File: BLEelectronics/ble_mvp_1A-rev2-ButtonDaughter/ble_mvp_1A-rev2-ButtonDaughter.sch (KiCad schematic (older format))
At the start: 7 parts, among them J1 Nordic_nRF52840_breakout, SW1 SW_Push, SW2 SW_Push, U1 BAT-HLD-001

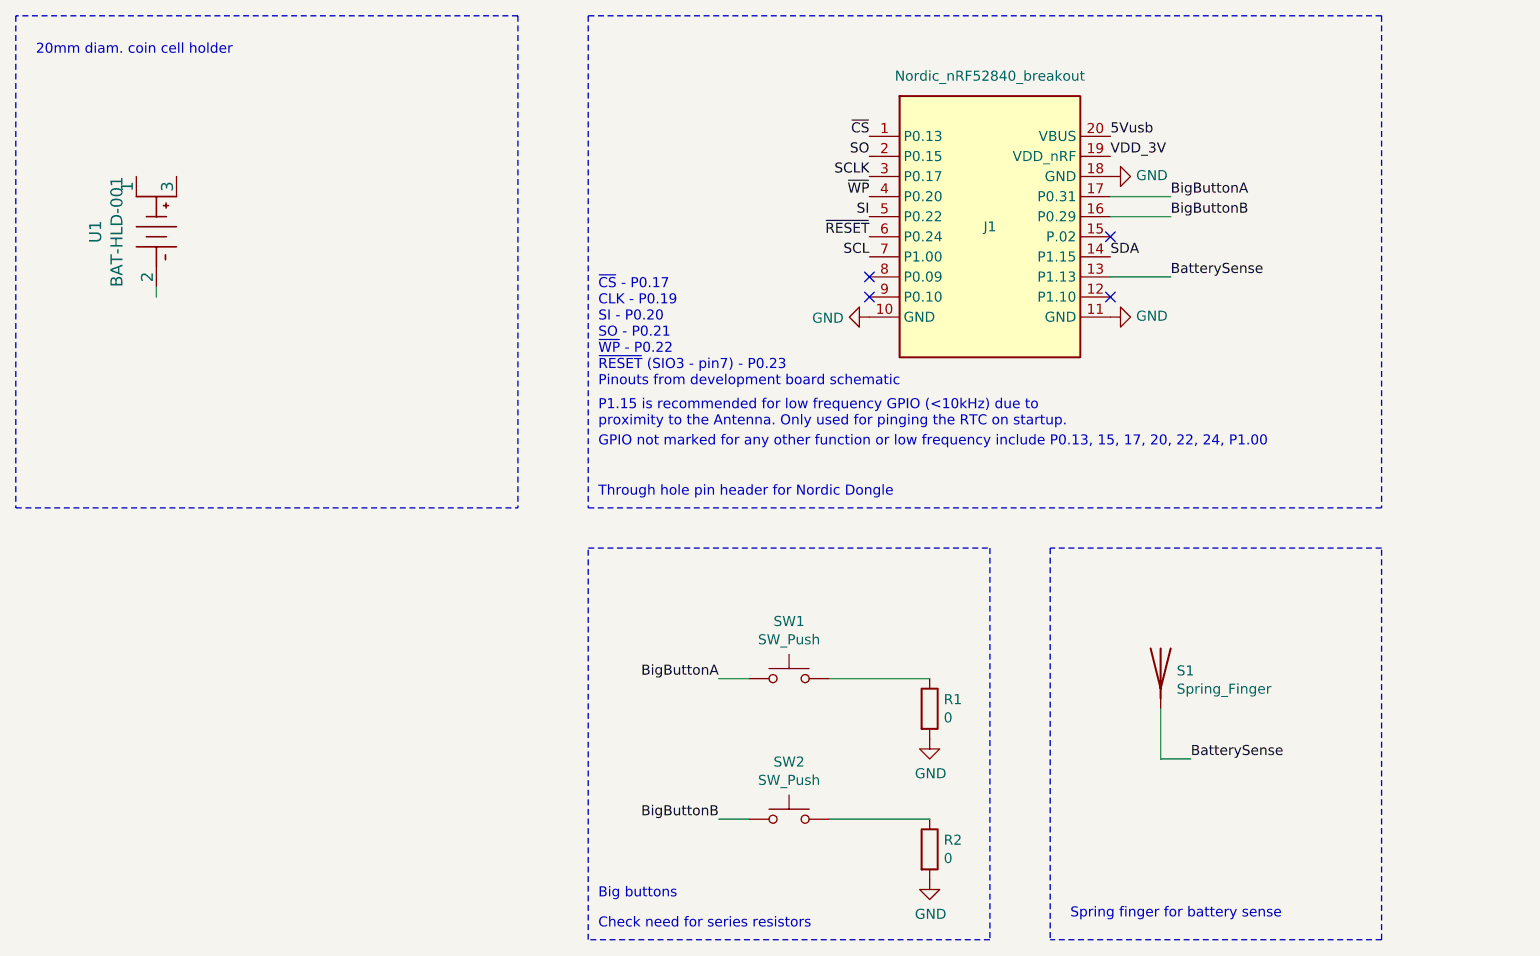
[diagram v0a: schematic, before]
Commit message: mvp1a-rev2 button daughter board schematic and layout ready for review. ToDo: BOM prep.
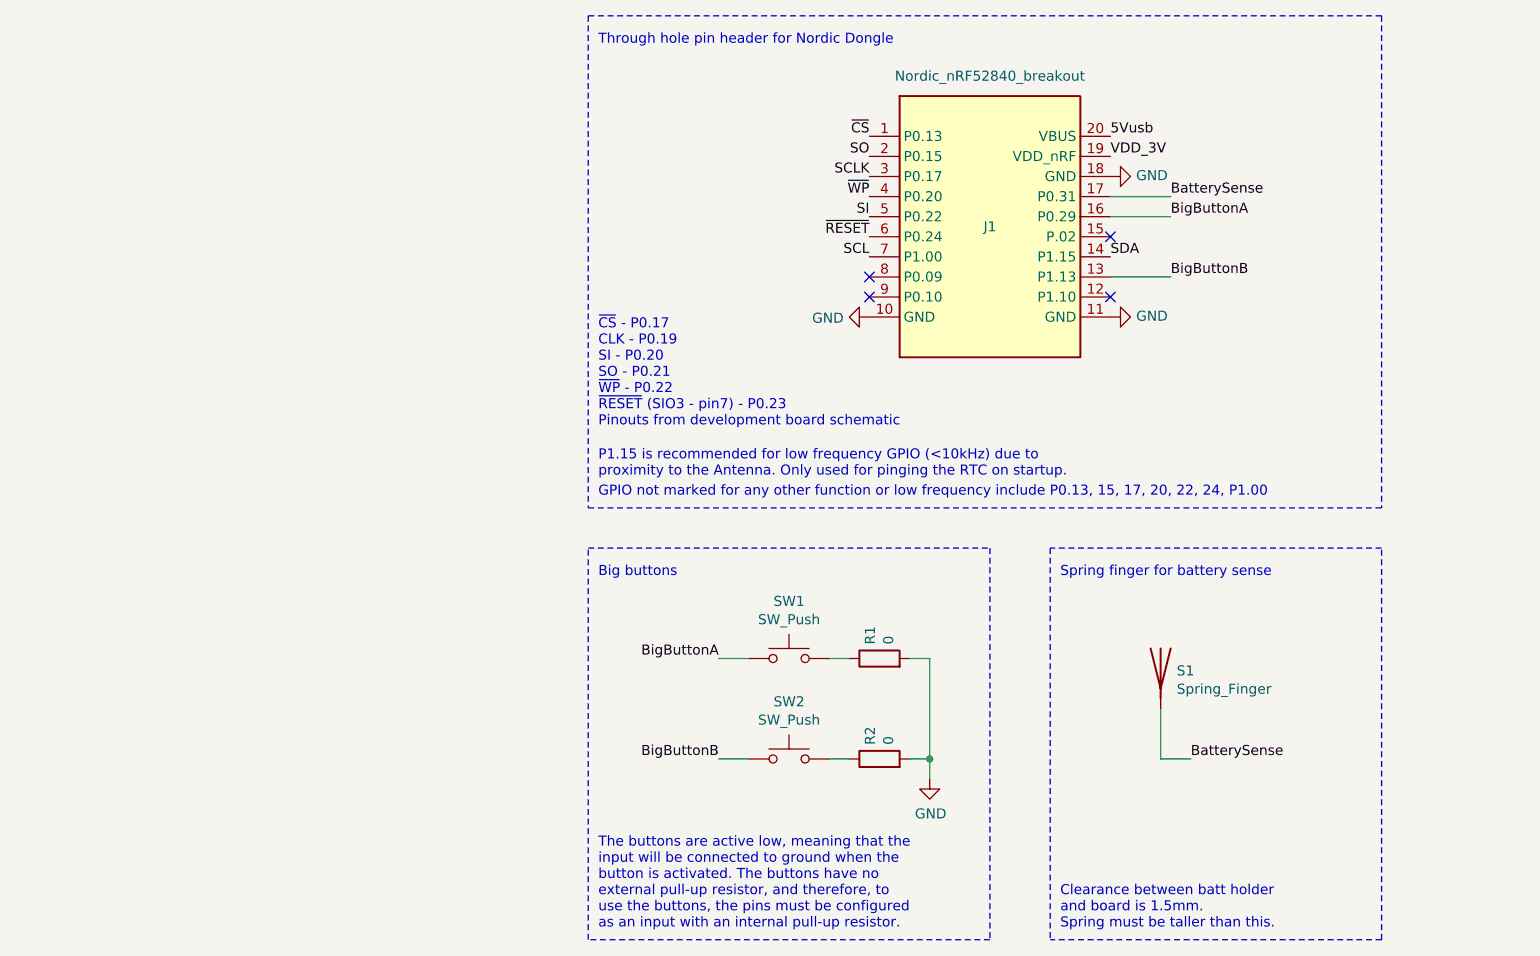
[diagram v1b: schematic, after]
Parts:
- removed U1: BAT-HLD-001, 0my_footprints:BAT-HLD-001, symbol BAT-HLD-001:BAT-HLD-001
- S1: footprint (none) -> 0my_footprints:SpringFingerGeneric; DPN (none) -> 952-2733-1-ND; MFR (none) -> Harwin Inc.; MPN (none) -> S7131-45R
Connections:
- wire segments 10 -> 13
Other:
- note added: "Clearance between batt holder \nand board is 1.5mm. \nSpring must be taller than this."
- note added: "The buttons are active low, meaning that the \ninput will be connected to ground when the\nbutton is activated. The buttons have no \nexternal pull-up resistor, and therefore, to \nuse the buttons, the pins must be configured \nas an input with an internal pull-up resistor."
- note removed: "20mm diam. coin cell holder"
- note removed: "Check need for series resistors"
- moved on the sheet: R1, R2, SW1, SW2
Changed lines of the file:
@@
 $EndDescr
 Wire Notes Line
-	1050 3350 3550 3350
-Wire Notes Line
-	3550 900  1050 900
-Wire Notes Line
 	7850 900  3900 900
 Wire Notes Line
-	3900 3350 7850 3350
-Wire Notes Line
-	3900 3550 5900 3550
-Wire Notes Line
 	5900 3550 5900 5500
 Wire Notes Line
@@
 Wire Notes Line
 	3900 900  3900 3350
-Wire Notes Line
-	3550 900  3550 3350
-Wire Notes Line
-	1050 900  1050 3350
 NoConn ~ 5300 2200
 NoConn ~ 6500 2000
 NoConn ~ 6500 2300
 NoConn ~ 5300 2300
-Text Notes 3950 3300 0    50   ~ 0
+Text Notes 3950 1050 0    50   ~ 0
 Through hole pin header for Nordic Dongle
 Text Label 6500 2100 0    50   ~ 0
@@
 Text Label 5300 2100 2    50   ~ 0
 SCL
-Text Notes 3950 2750 0    50   ~ 0
-~CS~ - P0.17\nCLK - P0.19\nSI - P0.20\nSO - P0.21\n~WP~ - P0.22\n~RESET~ (SIO3 - pin7) - P0.23\nPinouts from development board schematic\n
 Text Label 5300 2000 2    50   ~ 0
 ~RESET~
 Text Label 5300 1800 2    50   ~ 0
 ~WP~
-Text Notes 3950 2950 0    50   ~ 0
-P1.15 is recommended for low frequency GPIO (<10kHz) due to\nproximity to the Antenna. Only used for pinging the RTC on startup.
 Text Label 5300 1700 2    50   ~ 0
 SCLK
@@
 Text Label 5300 1600 2    50   ~ 0
 SO
-Text Notes 3950 3050 0    50   ~ 0
-GPIO not marked for any other function or low frequency include P0.13, 15, 17, 20, 22, 24, P1.00
 Text Label 6500 1600 0    50   ~ 0
 VDD_3V
@@
 	0    -1   -1   0
 $EndComp
-Wire Wire Line
-	1750 2300 1750 2250
-Text Notes 1150 1100 0    50   ~ 0
-20mm diam. coin cell holder
-$Comp
-L BAT-HLD-001:BAT-HLD-001 U1
-U 1 1 5E9C706C
-P 1650 1700
-F 0 "U1" H 1925 1903 60  0000 C CNN
-F 1 "BAT-HLD-001" H 1925 1797 60  0000 C CNN
-F 2 "0my_footprints:BAT-HLD-001" H 1934 1358 60  0001 C CNN
-F 3 "https://linxtechnologies.com/wp/wp-content/uploads/catalog-battery-holders.pdf" H 1650 1700 60  0001 C CNN
-F 4 "Linx Technologies Inc." H 0   0   50  0001 C CNN "MFR"
-F 5 "BAT-HLD-001" H 0   0   50  0001 C CNN "MPN"
-F 6 "BAT-HLD-001-ND" H 0   0   50  0001 C CNN "DPN"
-F 7 "-" H 0   0   50  0001 C CNN "LCSCPN"
-F 8 "-" H 0   0   50  0001 C CNN "SPR"
-F 9 "-" H 0   0   50  0001 C CNN "SPN"
-F 10 "-" H 0   0   50  0001 C CNN "SIM"
-	1    1650 1700
-	0    -1   1    0
-$EndComp
 $Comp
 L Switch:SW_Push SW1
 U 1 1 5ED9F9E5
-P 4900 4200
-F 0 "SW1" H 4900 4485 50  0000 C CNN
-F 1 "SW_Push" H 4900 4394 50  0000 C CNN
-F 2 "0my_footprints:TS-1187A-SMD_button" H 4900 4400 50  0001 C CNN
-F 3 "~" H 4900 4400 50  0001 C CNN
-	1    4900 4200
+P 4900 4100
+F 0 "SW1" H 4900 4385 50  0000 C CNN
+F 1 "SW_Push" H 4900 4294 50  0000 C CNN
+F 2 "0my_footprints:TS-1187A-SMD_button" H 4900 4300 50  0001 C CNN
+F 3 "~" H 4900 4300 50  0001 C CNN
+	1    4900 4100
 	1    0    0    -1
 $EndComp
@@
 L Switch:SW_Push SW2
 U 1 1 5ED9FE93
-P 4900 4900
-F 0 "SW2" H 4900 5185 50  0000 C CNN
-F 1 "SW_Push" H 4900 5094 50  0000 C CNN
-F 2 "0my_footprints:TS-1187A-SMD_button" H 4900 5100 50  0001 C CNN
-F 3 "~" H 4900 5100 50  0001 C CNN
-	1    4900 4900
+P 4900 4600
+F 0 "SW2" H 4900 4885 50  0000 C CNN
+F 1 "SW_Push" H 4900 4794 50  0000 C CNN
+F 2 "0my_footprints:TS-1187A-SMD_button" H 4900 4800 50  0001 C CNN
+F 3 "~" H 4900 4800 50  0001 C CNN
+	1    4900 4600
 	1    0    0    -1
 $EndComp
 Text Notes 3950 5450 0    50   ~ 0
-Check need for series resistors
-Text Notes 3950 5300 0    50   ~ 0
+The buttons are active low, meaning that the \ninput will be connected to ground when the\nbutton is activated. The buttons have no \nexternal pull-up resistor, and therefore, to \nuse the buttons, the pins must be configured \nas an input with an internal pull-up resistor.
+Text Notes 3950 3700 0    50   ~ 0
 Big buttons
-$Comp
-L Device:R R1
-U 1 1 5EDA175A
-P 5600 4350
-F 0 "R1" H 5670 4396 50  0000 L CNN
-F 1 "0" H 5670 4305 50  0000 L CNN
-F 2 "Resistor_SMD:R_0603_1608Metric" V 5530 4350 50  0001 C CNN
-F 3 "~" H 5600 4350 50  0001 C CNN
-	1    5600 4350
-	1    0    0    -1
-$EndComp
 $Comp
 L Device:R R2
 U 1 1 5EDA2493
-P 5600 5050
-F 0 "R2" H 5670 5096 50  0000 L CNN
-F 1 "0" H 5670 5005 50  0000 L CNN
-F 2 "Resistor_SMD:R_0603_1608Metric" V 5530 5050 50  0001 C CNN
-F 3 "~" H 5600 5050 50  0001 C CNN
-	1    5600 5050
-	1    0    0    -1
-$EndComp
-Wire Wire Line
-	4700 4200 4550 4200
-Wire Wire Line
-	4700 4900 4550 4900
-Wire Wire Line
-	5100 4200 5600 4200
-Wire Wire Line
-	5100 4900 5600 4900
-$Comp
-L power:GND #PWR0101
-U 1 1 5EDA3402
-P 5600 4500
-F 0 "#PWR0101" H 5600 4250 50  0001 C CNN
-F 1 "GND" H 5605 4327 50  0000 C CNN
-F 2 "" H 5600 4500 50  0001 C CNN
-F 3 "" H 5600 4500 50  0001 C CNN
-	1    5600 4500
-	1    0    0    -1
-$EndComp
+P 5350 4600
+F 0 "R2" H 5420 4646 50  0000 L CNN
+F 1 "0" H 5420 4555 50  0000 L CNN
+F 2 "Resistor_SMD:R_0603_1608Metric" V 5280 4600 50  0001 C CNN
+F 3 "~" H 5350 4600 50  0001 C CNN
+	1    5350 4600
+	0    -1   -1   0
+$EndComp
+Wire Wire Line
+	4700 4100 4550 4100
+Wire Wire Line
+	4700 4600 4550 4600
 $Comp
 L power:GND #PWR0102
 U 1 1 5EDA3C8A
-P 5600 5200
-F 0 "#PWR0102" H 5600 4950 50  0001 C CNN
-F 1 "GND" H 5605 5027 50  0000 C CNN
-F 2 "" H 5600 5200 50  0001 C CNN
-F 3 "" H 5600 5200 50  0001 C CNN
-	1    5600 5200
-	1    0    0    -1
-$EndComp
-Text Label 6800 1800 0    50   ~ 0
+P 5600 4700
+F 0 "#PWR0102" H 5600 4450 50  0001 C CNN
+F 1 "GND" H 5605 4527 50  0000 C CNN
+F 2 "" H 5600 4700 50  0001 C CNN
+F 3 "" H 5600 4700 50  0001 C CNN
+	1    5600 4700
+	1    0    0    -1
+$EndComp
+Text Label 6800 1900 0    50   ~ 0
 BigButtonA
-Text Label 6800 1900 0    50   ~ 0
+Text Label 6800 2200 0    50   ~ 0
 BigButtonB
 Wire Wire Line
@@
 Wire Wire Line
 	6800 1900 6500 1900
-Text Label 4550 4200 2    50   ~ 0
+Text Label 4550 4100 2    50   ~ 0
 BigButtonA
-Text Label 4550 4900 2    50   ~ 0
+Text Label 4550 4600 2    50   ~ 0
 BigButtonB
 $Comp
@@
 F 0 "S1" H 6830 4139 50  0000 L CNN
 F 1 "Spring_Finger" H 6830 4048 50  0000 L CNN
-F 2 "" H 6750 4150 50  0001 C CNN
-F 3 "~" H 6750 4150 50  0001 C CNN
+F 2 "0my_footprints:SpringFingerGeneric" H 6750 4150 50  0001 C CNN
+F 3 "https://cdn.harwin.com/pdfs/S7131-45R.pdf" H 6750 4150 50  0001 C CNN
+F 4 "Harwin Inc." H 6750 4150 50  0001 C CNN "MFR"
+F 5 "S7131-45R" H 6750 4150 50  0001 C CNN "MPN"
+F 6 "952-2733-1-ND" H 6750 4150 50  0001 C CNN "DPN"
 	1    6750 4150
 	1    0    0    -1
 $EndComp
-Text Notes 6300 5400 0    50   ~ 0
+Text Notes 6250 3700 0    50   ~ 0
 Spring finger for battery sense
 Wire Notes Line
-	7850 3550 6200 3550
-Wire Notes Line
 	7850 5500 6200 5500
 Wire Wire Line
@@
 Wire Wire Line
 	6800 2200 6500 2200
-Text Label 6800 2200 0    50   ~ 0
+Text Label 6800 1800 0    50   ~ 0
 BatterySense
 Text Label 6900 4600 0    50   ~ 0
 BatterySense
+Text Notes 6250 5450 0    50   ~ 0
+Clearance between batt holder \nand board is 1.5mm. \nSpring must be taller than this.
+Wire Notes Line
+	7850 3550 6200 3550
+Wire Notes Line
+	3900 3550 5900 3550
+Text Notes 3950 3200 0    50   ~ 0
+P1.15 is recommended for low frequency GPIO (<10kHz) due to\nproximity to the Antenna. Only used for pinging the RTC on startup.
+Text Notes 3950 3300 0    50   ~ 0
+GPIO not marked for any other function or low frequency include P0.13, 15, 17, 20, 22, 24, P1.00
+Text Notes 3950 2950 0    50   ~ 0
+~CS~ - P0.17\nCLK - P0.19\nSI - P0.20\nSO - P0.21\n~WP~ - P0.22\n~RESET~ (SIO3 - pin7) - P0.23\nPinouts from development board schematic\n
+Wire Notes Line
+	3900 3350 7850 3350
+$Comp
+L Device:R R1
+U 1 1 5EDA175A
+P 5350 4100
+F 0 "R1" H 5420 4146 50  0000 L CNN
+F 1 "0" H 5420 4055 50  0000 L CNN
+F 2 "Resistor_SMD:R_0603_1608Metric" V 5280 4100 50  0001 C CNN
+F 3 "~" H 5350 4100 50  0001 C CNN
+	1    5350 4100
+	0    -1   -1   0
+$EndComp
+Wire Wire Line
+	5500 4100 5600 4100
+Wire Wire Line
+	5200 4100 5100 4100
+Wire Wire Line
+	5600 4100 5600 4600
+Wire Wire Line
+	5500 4600 5600 4600
+Connection ~ 5600 4600
+Wire Wire Line
+	5600 4600 5600 4700
+Wire Wire Line
+	5200 4600 5100 4600
 $EndSCHEMATC

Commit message: mvp1a-rev2 button daughter board BOM clean.
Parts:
- R1, R2: LCSCPN (none) -> C21189; MFR (none) -> Uniroyal Elec; MPN (none) -> 0603WAF0000T5E
- SW1, SW2: LCSCPN (none) -> C318886; MFR (none) -> XKB Enterprise; MPN (none) -> TS-1187A-C-G-B
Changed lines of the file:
@@
 F 1 "SW_Push" H 4900 4294 50  0000 C CNN
 F 2 "0my_footprints:TS-1187A-SMD_button" H 4900 4300 50  0001 C CNN
-F 3 "~" H 4900 4300 50  0001 C CNN
+F 3 "https://datasheet.lcsc.com/szlcsc/2002271432_XKB-Enterprise-TS-1187A-C-G-B_C318886.pdf" H 4900 4300 50  0001 C CNN
+F 4 "XKB Enterprise" H 4900 4100 50  0001 C CNN "MFR"
+F 5 "TS-1187A-C-G-B" H 4900 4100 50  0001 C CNN "MPN"
+F 6 "C318886" H 4900 4100 50  0001 C CNN "LCSCPN"
 	1    4900 4100
 	1    0    0    -1
@@
 F 1 "SW_Push" H 4900 4794 50  0000 C CNN
 F 2 "0my_footprints:TS-1187A-SMD_button" H 4900 4800 50  0001 C CNN
-F 3 "~" H 4900 4800 50  0001 C CNN
+F 3 "https://datasheet.lcsc.com/szlcsc/2002271432_XKB-Enterprise-TS-1187A-C-G-B_C318886.pdf" H 4900 4800 50  0001 C CNN
+F 4 "XKB Enterprise" H 4900 4600 50  0001 C CNN "MFR"
+F 5 "TS-1187A-C-G-B" H 4900 4600 50  0001 C CNN "MPN"
+F 6 "C318886" H 4900 4600 50  0001 C CNN "LCSCPN"
 	1    4900 4600
 	1    0    0    -1
@@
 F 1 "0" H 5420 4555 50  0000 L CNN
 F 2 "Resistor_SMD:R_0603_1608Metric" V 5280 4600 50  0001 C CNN
-F 3 "~" H 5350 4600 50  0001 C CNN
+F 3 "https://datasheet.lcsc.com/szlcsc/Uniroyal-Elec-0603WAF0000T5E_C21189.pdf" H 5350 4600 50  0001 C CNN
+F 4 "Uniroyal Elec" H 5350 4600 50  0001 C CNN "MFR"
+F 5 "0603WAF0000T5E" H 5350 4600 50  0001 C CNN "MPN"
+F 6 "C21189" H 5350 4600 50  0001 C CNN "LCSCPN"
 	1    5350 4600
 	0    -1   -1   0
@@
 F 1 "0" H 5420 4055 50  0000 L CNN
 F 2 "Resistor_SMD:R_0603_1608Metric" V 5280 4100 50  0001 C CNN
-F 3 "~" H 5350 4100 50  0001 C CNN
+F 3 "https://datasheet.lcsc.com/szlcsc/Uniroyal-Elec-0603WAF0000T5E_C21189.pdf" H 5350 4100 50  0001 C CNN
+F 4 "Uniroyal Elec" H 5350 4100 50  0001 C CNN "MFR"
+F 5 "0603WAF0000T5E" H 5350 4100 50  0001 C CNN "MPN"
+F 6 "C21189" H 5350 4100 50  0001 C CNN "LCSCPN"
 	1    5350 4100
 	0    -1   -1   0
